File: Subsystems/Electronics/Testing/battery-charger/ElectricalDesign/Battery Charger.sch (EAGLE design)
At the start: 139 parts, among them J1 USB4515-GF-A_REVA, J3 10103592-0001LF, Q1 CSD16406Q3, Q2 CSD16406Q3, Q3 DMN2008LFU, Q4 DMN2008LFU, Q5 DMN2008LFU, Q6 BC817, Q7 BC817, Q8 DMN53D0L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

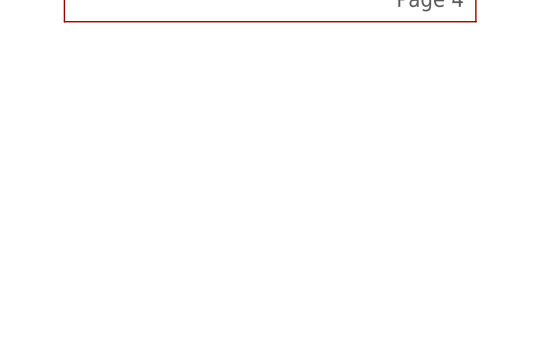
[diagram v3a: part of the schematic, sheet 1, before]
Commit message: Added Signature
Added personal (Zachary) signature to library, schematic, and board. Also added LED color code text to physical board
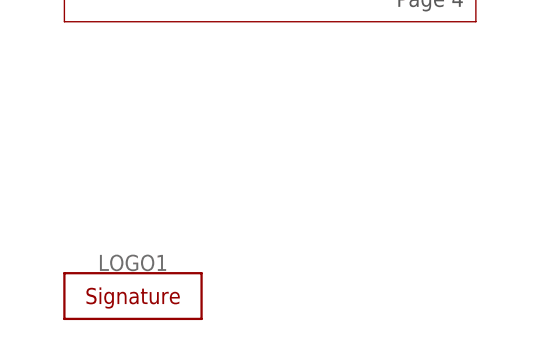
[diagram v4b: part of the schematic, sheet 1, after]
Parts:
- added LOGO1: SIGNATUREZACHARY, CougsInSpace-Aesthetics:SIGNATUREZACHARY
- renumbered TP11-CN2102N_VDD to TP11-CP2102N_VDD
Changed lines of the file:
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@@
 <part name="TP9-TEMP_C" library="CougsInSpace-Connectors" deviceset="TEST_POINT" device="-SMD-C-1.25"/>
 <part name="TP10-USB_5.0V" library="CougsInSpace-Connectors" deviceset="TEST_POINT" device="-SMD-C-1.25"/>
-<part name="TP11-CN2102N_VDD" library="CougsInSpace-Connectors" deviceset="TEST_POINT" device="-SMD-C-1.25"/>
+<part name="TP11-CP2102N_VDD" library="CougsInSpace-Connectors" deviceset="TEST_POINT" device="-SMD-C-1.25"/>
 <part name="TP12-3.3V" library="CougsInSpace-Connectors" deviceset="TEST_POINT" device="-SMD-C-1.25"/>
 <part name="R42" library="CougsInSpace-Resistors" deviceset="RES-V" device="-1608" technology="-0" value="0Ω &lt;20mΩ"/>
@@
 <part name="SUPPLY87" library="CougsInSpace-PowerSymbols" deviceset="5.0V" device=""/>
 <part name="SUPPLY88" library="CougsInSpace-PowerSymbols" deviceset="3.3V" device=""/>
+<part name="LOGO1" library="CougsInSpace-Aesthetics" deviceset="SIGNATURE" device="ZACHARY"/>
 </parts>
 <sheets>
@@
 <attribute name="PART_NUMBER" x="219.71" y="24.13" size="3.81" layer="94" ratio="15" align="bottom-right"/>
 </instance>
+<instance part="LOGO1" gate="G$1" x="-15.24" y="22.86" smashed="yes">
+<attribute name="NAME" x="-15.24" y="25.654" size="1.778" layer="95" align="bottom-center"/>
+</instance>
 </instances>
 <busses>
@@
 <attribute name="NAME" x="28.956" y="123.444" size="1.27" layer="95" align="center-left"/>
 </instance>
-<instance part="TP11-CN2102N_VDD" gate="G$1" x="142.24" y="139.7" smashed="yes">
+<instance part="TP11-CP2102N_VDD" gate="G$1" x="142.24" y="139.7" smashed="yes">
 <attribute name="NAME" x="140.716" y="141.224" size="1.27" layer="95" align="center-left"/>
 </instance>
@@
 <junction x="144.78" y="137.16"/>
 <wire x1="144.78" y1="139.7" x2="142.24" y2="139.7" width="0.1524" layer="91"/>
-<pinref part="TP11-CN2102N_VDD" gate="G$1" pin="1"/>
-</segment>
-</net>
+<pinref part="TP11-CP2102N_VDD" gate="G$1" pin="1"/>
+</segment>
+</net>
